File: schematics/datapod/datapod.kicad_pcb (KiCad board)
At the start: 2 copper layers, 152.7 x 152.7 mm, 61 parts, among them J1 Conn_01x02, J2 Conn_02x03_Odd_Even, J3 Conn_01x02, J4 DB9_Female, J5 DB9_Male_MountingHoles, J6 Micro_SD_Card, J7 Conn_02x02_Odd_Even, J8 Conn_01x02_Female, J9 Conn_02x03_Odd_Even, K1 DS2E-SL2-DC5V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

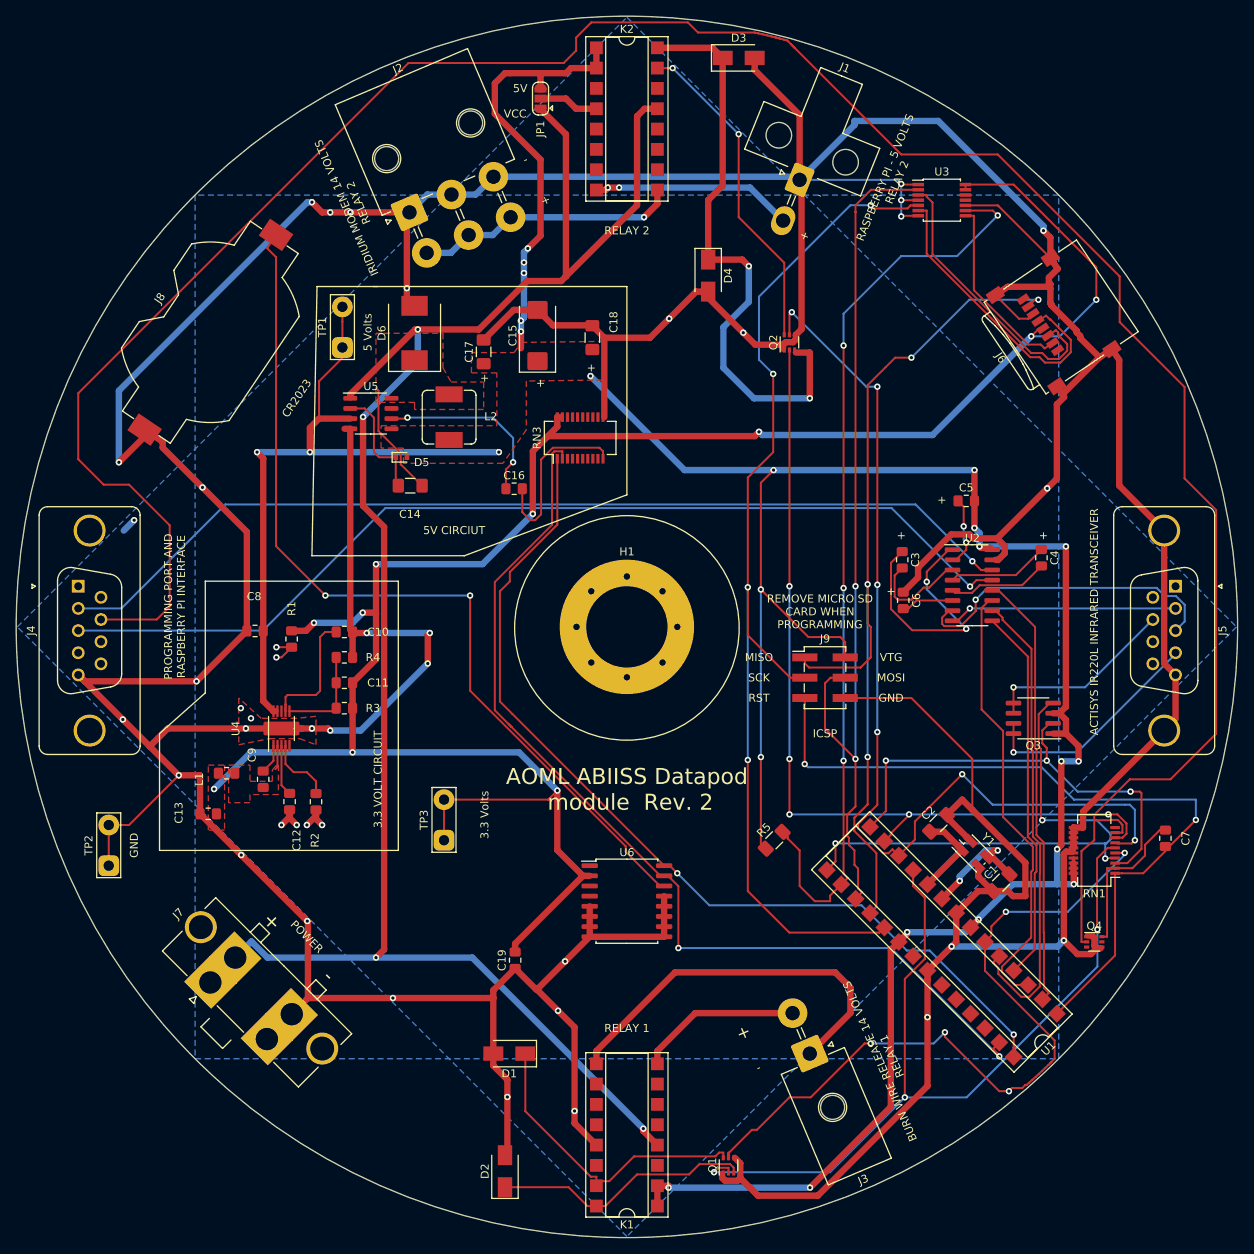
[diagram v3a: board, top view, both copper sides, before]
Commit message: added rtc stuff , rotated db9s , added on/off transistors for max chip and sdcard
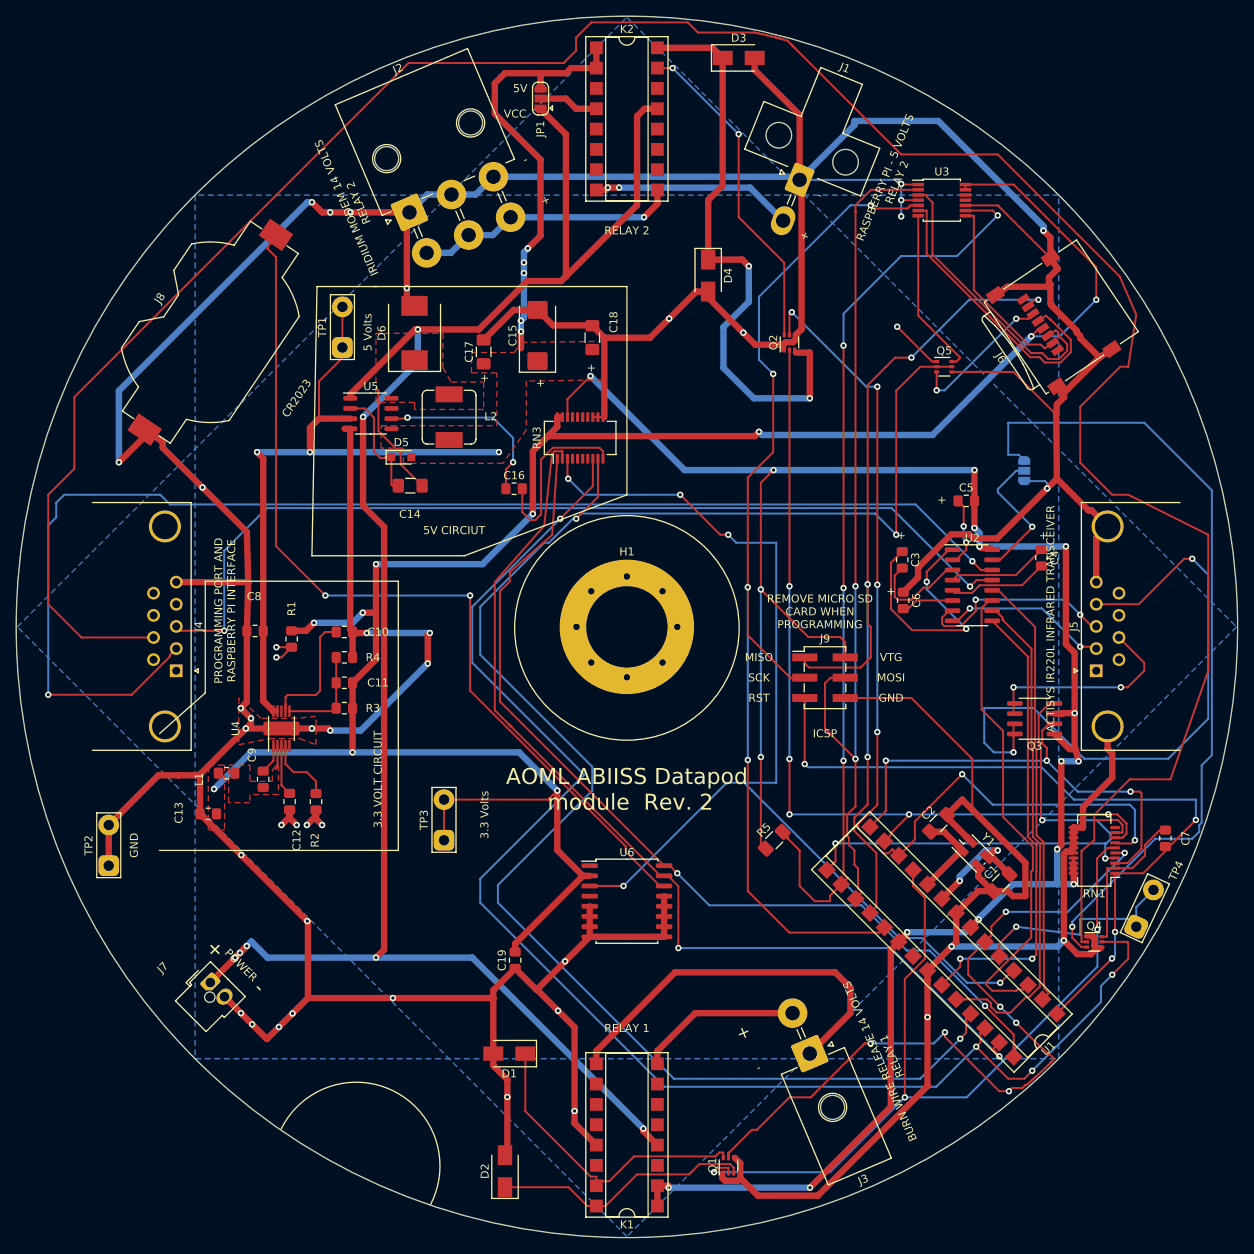
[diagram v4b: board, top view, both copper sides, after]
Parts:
- added JP2: SolderJumper_3_Open, Jumper:SolderJumper-3_P1.3mm_Open_RoundedPad1.0x1.5mm, B.Cu at (150.0, 77.0)
- added Q5: FDG1024NZ, Package_TO_SOT_SMD:SOT-363_SC-70-6, F.Cu at (140.0, 64.0)
- added TP4: TestPoint_2Pole, TestPoint:TestPoint_2Pads_Pitch5.08mm_Drill1.3mm, F.Cu at (164.0, 134.0)
- D5: value 1N914BWT -> CMDSH-3; footprint Diode_SMD:D_SOD-523 -> Diode_SMD:D_SOD-323_HandSoldering
- J4: footprint Connector_Dsub:DSUB-9_Female_Vertical_P2.77x2.84mm_MountingHoles -> Connector_Dsub:DSUB-9_Female_Horizontal_P2.77x2.84mm_EdgePinOffset7.70mm_Housed_MountingHolesOffset9.12mm
- J5: footprint Connector_Dsub:DSUB-9_Male_Vertical_P2.77x2.84mm_MountingHoles -> Connector_Dsub:DSUB-9_Male_Horizontal_P2.77x2.84mm_EdgePinOffset7.70mm_Housed_MountingHolesOffset9.12mm
- J7: footprint Connector_Molex:Molex_Mini-Fit_Sr_42819-22XX_1x02_P10.00mm_Vertical -> Connector_Molex:Molex_Nano-Fit_105309-xx02_1x02_P2.50mm_Vertical
- moved J4 16.2 mm to (44.0, 102.0), turned to 270 degrees
- moved J5 14.5 mm to (159.0, 102.0), turned to 90 degrees
- moved Q3 0.18 mm to (151.3, 108.0)
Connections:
- J6 pad 6: GND -> Net-(J6-Pad6)
- Q4 pad 5: Net-(Q4-Pad5) -> RS232_DRIVER_ON_OFF
- RN3 pad 12: Net-(RN3-Pad12) -> GND
- RN3 pad 13: Net-(RN3-Pad13) -> GND
- RN3 pad 18: Net-(RN3-Pad18) -> +5V
- RN3 pad 3: Net-(RN3-Pad3) -> RTC_~INT~_SQW
- RN3 pad 8: Net-(RN3-Pad8) -> RS232_DRIVER_ON_OFF
- RN3 pad 9: Net-(RN3-Pad9) -> uSD_ON_OFF
- U1 pad 23: Net-(U1-Pad23) -> MCU-VIRT-UART-RX
- U1 pad 24: Net-(U1-Pad24) -> MCU-SOFT-UART-TX
- U1 pad 25: Net-(U1-Pad25) -> uSD_ON_OFF
- U1 pad 26: Net-(U1-Pad26) -> RS232_DRIVER_ON_OFF
- U1 pad 4: MCU-VIRT-UART-RX -> RTC_~INT~_SQW
- U1 pad 5: MCU-SOFT-UART-TX -> Net-(TP4-Pad1)
- U2 pad 15: GND -> Net-(JP2-Pad2)
- U3 pad 7: GND -> Net-(Q5-Pad6)
- U6 pad 3: Net-(U6-Pad3) -> RTC_~INT~_SQW
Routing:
- net uSD_ON_OFF: track 0.00 -> 213.1 mm, vias 0 -> 3
- net RS232_DRIVER_ON_OFF: track 0.00 -> 182.7 mm, vias 0 -> 4
- net RTC_~INT~_SQW: track 0.00 -> 135.2 mm, vias 0 -> 5
- net Net-(JP2-Pad3): track 0.00 -> 103.4 mm, vias 0 -> 1
- net /SERIAL COMMUNICATIONS SHEET/DTR_ON: track 29.1 -> 80.0 mm, vias 1 -> 2
- net GND: track 947.3 -> 905.1 mm, vias 41 -> 42
- net Net-(J4-Pad2): track 123.4 -> 164.6 mm, vias 1 -> 2
- net Net-(TP4-Pad1): track 0.00 -> 27.5 mm, vias 0 -> 1
- net Net-(Q5-Pad6): track 0.00 -> 21.2 mm
- net Net-(J6-Pad6): track 0.00 -> 18.3 mm, vias 0 -> 2
- net Net-(JP2-Pad2): track 0.00 -> 17.5 mm, vias 0 -> 1
- net Net-(J5-Pad3): track 40.5 -> 25.6 mm, vias 1 -> 2
- net MCU-VIRT-UART-RX: track 47.2 -> 58.0 mm, vias 0 -> 2
- net +5V: track 416.2 -> 425.3 mm, vias 24 -> 25
- net Net-(J5-Pad2): track 28.5 -> 20.7 mm, vias 1 -> 2
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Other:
- board text added: "trans"
